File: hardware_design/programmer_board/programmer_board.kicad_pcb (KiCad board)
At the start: 2 copper layers, 27 parts, among them J1 SM06B-SRSS-TB(LF)(SN), J2 USB4800-03-A_REVA, Q1 SS8050-G, Q2 SS8050-G, U1 AP2112K-3.3TRG1, U2 TPD2S017DBVR, U3 CH340G, Y1 ECS-120-20-3X-EN-TR

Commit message: Almost routed programmer board
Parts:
- moved D1 46.7 mm to (99.3, 86.4)
- moved R3 38.2 mm to (99.3, 88.1)
- moved Q2 30.1 mm to (117.9, 95.8)
- moved R2 25.6 mm to (114.8, 92.2)
- moved C4 24.9 mm to (110.5, 90.4), turned to 180 degrees
- moved C3 24.5 mm to (110.5, 88.4), turned to 180 degrees
- moved Q1 24.1 mm to (117.9, 100.2)
- moved R1 22.3 mm to (121.4, 92.2)
- moved J1 17.1 mm to (125.3, 89.7)
- moved R4 16.3 mm to (118.1, 92.2), turned to 180 degrees
- moved C8 12.9 mm to (121.0, 96.5), turned to 90 degrees
- moved S1 12.1 mm to (125.0, 96.5), turned to 180 degrees
- moved S2 11.9 mm to (125.0, 100.1), turned to 180 degrees
- moved C9 11.9 mm to (120.9, 100.1), turned to 90 degrees
- moved Y1 11.2 mm to (106.4, 89.4)
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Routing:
- net GND: track 7.85 -> 36.5 mm, vias 3 -> 9
- net RST: track 0.00 -> 22.8 mm, vias 0 -> 2
- net BOOT: track 0.00 -> 20.4 mm
- net RTS: track 0.00 -> 18.5 mm
- net DTR: track 0.00 -> 13.6 mm
- net /USB_N: track 11.6 -> 25.0 mm
- net Net-(U3-XO): track 0.00 -> 13.2 mm
- net VBUS: track 22.7 -> 32.8 mm, vias 0 -> 2
- net /USB_P: track 14.7 -> 24.7 mm
- net Net-(C5-Pad1): track 7.80 -> 15.6 mm
- net Net-(U3-XI): track 0.00 -> 7.14 mm
- net Net-(J2-CC2): track 0.00 -> 6.66 mm
- net Net-(J2-CC1): track 0.00 -> 6.61 mm
- net +3.3V: track 11.0 -> 15.6 mm
- net Net-(J1-Pad1): track 0.00 -> 3.03 mm
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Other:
- board text added: "BOOT"
- board text added: "RST"

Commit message: Programmer board progress
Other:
- board outline added: 47.5 x 18.5 mm
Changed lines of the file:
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@@
     (pad "S2" smd rect (at 3.8 3.875 90) (size 1.2 1.8) (layers "F.Cu" "F.Paste" "F.Mask")
       (net 13 "Net-(J1-SHIELD-PadS1)") (pinfunction "SHIELD") (pintype "passive"))
+    (model "C:/Users/perry/Documents/Footprints/SM06B-SRSS-TB_LF__SN_/SM06B-SRSS-TB_LF__SN_.step"
+      (offset (xyz 0 -2 0))
+      (scale (xyz 1 1 1))
+      (rotate (xyz -90 0 0))
+    )
   )
   (footprint "SS8050-G:TRANS_SS8050-G" (layer "F.Cu")
@@
     (pad "3" smd rect (at 1.01 0) (size 0.8 0.6) (layers "F.Cu" "F.Paste" "F.Mask")
       (net 8 "RST") (pintype "passive"))
+    (model "C:/Users/perry/Documents/Footprints/SS8050-G/SS8050-G.step"
+      (offset (xyz 0 0 0))
+      (scale (xyz 1 1 1))
+      (rotate (xyz -90 0 0))
+    )
   )
   (footprint "TL6330AF200Q:SW_TL6330AF200Q" (layer "F.Cu")
@@
     (pad "4" smd rect (at 2.05 -0.8 180) (size 0.9 1) (layers "F.Cu" "F.Paste" "F.Mask")
       (net 8 "RST") (pintype "passive"))
+    (model "C:/Users/perry/Documents/Footprints/TL6330AF200Q/TL6330AF200Q.step"
+      (offset (xyz 0 0 0))
+      (scale (xyz 1 1 1))
+      (rotate (xyz -90 0 0))
+    )
   )
   (footprint "Resistor_SMD:R_0603_1608Metric" (layer "F.Cu")
@@
     (pad "16" smd roundrect (at 2.75 -4.445 270) (size 1.31 0.62) (layers "F.Cu" "F.Paste" "F.Mask") (roundrect_rratio 0.08)
       (net 1 "+3.3V") (pinfunction "VCC") (pintype "power_in"))
+    (model "C:/Users/perry/Documents/Footprints/CH340G/CH340G.step"
+      (offset (xyz 0 0 0))
+      (scale (xyz 1 1 1))
+      (rotate (xyz -90 0 0))
+    )
   )
   (footprint "Capacitor_SMD:C_0603_1608Metric" (layer "F.Cu")
@@
     (pad "5" smd roundrect (at 1.185 -0.95 270) (size 0.6 1.35) (layers "F.Cu" "F.Paste" "F.Mask") (roundrect_rratio 0.1)
       (net 1 "+3.3V") (pinfunction "VOUT") (pintype "power_in"))
+    (model "C:/Users/perry/Documents/Footprints/AP2112K-3.3TRG1/AP2112K-3.3TRG1.step"
+      (offset (xyz 0 0 0))
+      (scale (xyz 1 1 1))
+      (rotate (xyz -90 0 -90))
+    )
   )
   (footprint "TPD2S017DBVR:SOT95P280X145-6N" (layer "F.Cu")
@@
     (pad "6" smd roundrect (at 1.255 -0.95) (size 1.21 0.58) (layers "F.Cu" "F.Paste" "F.Mask") (roundrect_rratio 0.07)
       (net 28 "/USB_P") (pinfunction "CH2_OUT") (pintype "output"))
+    (model "C:/Users/perry/Documents/Footprints/TPD2S017DBVR/TPD2S017DBVR.step"
+      (offset (xyz 0 0 0))
+      (scale (xyz 1 1 1))
+      (rotate (xyz -90 0 0))
+    )
   )
   (footprint "Resistor_SMD:R_0603_1608Metric" (layer "F.Cu")
@@
     (pad "4" smd rect (at 2.05 -0.8 180) (size 0.9 1) (layers "F.Cu" "F.Paste" "F.Mask")
       (net 7 "BOOT") (pintype "passive"))
+    (model "C:/Users/perry/Documents/Footprints/TL6330AF200Q/TL6330AF200Q.step"
+      (offset (xyz 0 0 0))
+      (scale (xyz 1 1 1))
+      (rotate (xyz -90 0 0))
+    )
   )
   (footprint "Resistor_SMD:R_0603_1608Metric" (layer "F.Cu")
@@
     (pad "3" smd rect (at 1.01 0) (size 0.8 0.6) (layers "F.Cu" "F.Paste" "F.Mask")
       (net 7 "BOOT") (pintype "passive"))
+    (model "C:/Users/perry/Documents/Footprints/SS8050-G/SS8050-G.step"
+      (offset (xyz 0 0 0))
+      (scale (xyz 1 1 1))
+      (rotate (xyz -90 0 0))
+    )
   )
   (footprint "Resistor_SMD:R_0603_1608Metric" (layer "F.Cu")
@@
     (property "Sheetname" "")
     (attr smd)
-    (fp_text reference "J2" (at 3.0635 -7.112 -180) (layer "F.SilkS") hide
-        (effects (font (size 1 1) (thickness 0.15)))
-    )
-    (fp_text value "USB4800-03-A_REVA" (at 7.975 -7.635 -90) (layer "F.Fab")
-        (effects (font (size 1 1) (thickness 0.15)))
-    )
-    (fp_text user "PCB EDGE" (at 5.5 1.9 -90) (layer "F.Fab")
+    (fp_text reference "J2" (at 3.0635 -7.112) (layer "F.SilkS") hide
+        (effects (font (size 1 1) (thickness 0.15)))
+    )
+    (fp_text value "USB4800-03-A_REVA" (at 7.975 -7.635 90) (layer "F.Fab")
+        (effects (font (size 1 1) (thickness 0.15)))
+    )
+    (fp_text user "PCB EDGE" (at 5.5 1.9 90) (layer "F.Fab")
         (effects (font (size 0.64 0.64) (thickness 0.15)))
     )
@@
     (pad "S4" thru_hole oval (at 4.61 -4.5 270) (size 1 2) (drill oval 0.6 1.6) (layers "*.Cu" "*.Mask")
       (net 14 "Net-(J2-SHIELD-PadS1)") (pinfunction "SHIELD") (pintype "passive"))
+    (model "C:/Users/perry/Documents/Footprints/USB4800-03-A_REVA/USB4800-03-A_REVA.step"
+      (offset (xyz 0 0 0))
+      (scale (xyz 1 1 1))
+      (rotate (xyz -90 0 0))
+    )
   )
   (footprint "Inductor_SMD:L_0805_2012Metric" (layer "F.Cu")
@@
     (pad "2" smd rect (at 2.75 0 270) (size 3.5 1.2) (layers "F.Cu" "F.Paste" "F.Mask")
       (net 5 "Net-(U3-XI)") (pintype "passive"))
-  )
+    (model "C:/Users/perry/Documents/Footprints/ECS-122.8-20-3X-EN-TR/ECS-122.8-20-3X-EN-TR.step"
+      (offset (xyz 0 0 0))
+      (scale (xyz 1 1 1))
+      (rotate (xyz -90 0 0))
+    )
+  )
+  (gr_line (start 83.448026 85.852) (end 83.439 101.854)
+    (stroke (width 0.1) (type default)) (layer "Edge.Cuts"))
+  (gr_line (start 130.927974 101.854) (end 130.927974 85.852)
+    (stroke (width 0.1) (type default)) (layer "Edge.Cuts"))
+  (gr_arc (start 130.927974 101.854) (mid 130.556 102.752026) (end 129.657974 103.124)
+    (stroke (width 0.1) (type default)) (layer "Edge.Cuts"))
+  (gr_arc (start 83.448026 85.852) (mid 83.82 84.953974) (end 84.718026 84.582)
+    (stroke (width 0.1) (type default)) (layer "Edge.Cuts"))
+  (gr_arc (start 84.709 103.124) (mid 83.810974 102.752026) (end 83.439 101.854)
+    (stroke (width 0.1) (type default)) (layer "Edge.Cuts"))
+  (gr_arc (start 129.657974 84.582) (mid 130.556 84.953974) (end 130.927974 85.852)
+    (stroke (width 0.1) (type default)) (layer "Edge.Cuts"))
+  (gr_line (start 84.709 103.124) (end 129.657974 103.124)
+    (stroke (width 0.1) (type default)) (layer "Edge.Cuts"))
+  (gr_line (start 84.718026 84.582) (end 129.657974 84.582)
+    (stroke (width 0.1) (type default)) (layer "Edge.Cuts"))
   (gr_text "RST" (at 130.0755 101.816 90) (layer "F.SilkS")
     (effects (font (size 1 1) (thickness 0.25) bold) (justify left bottom))

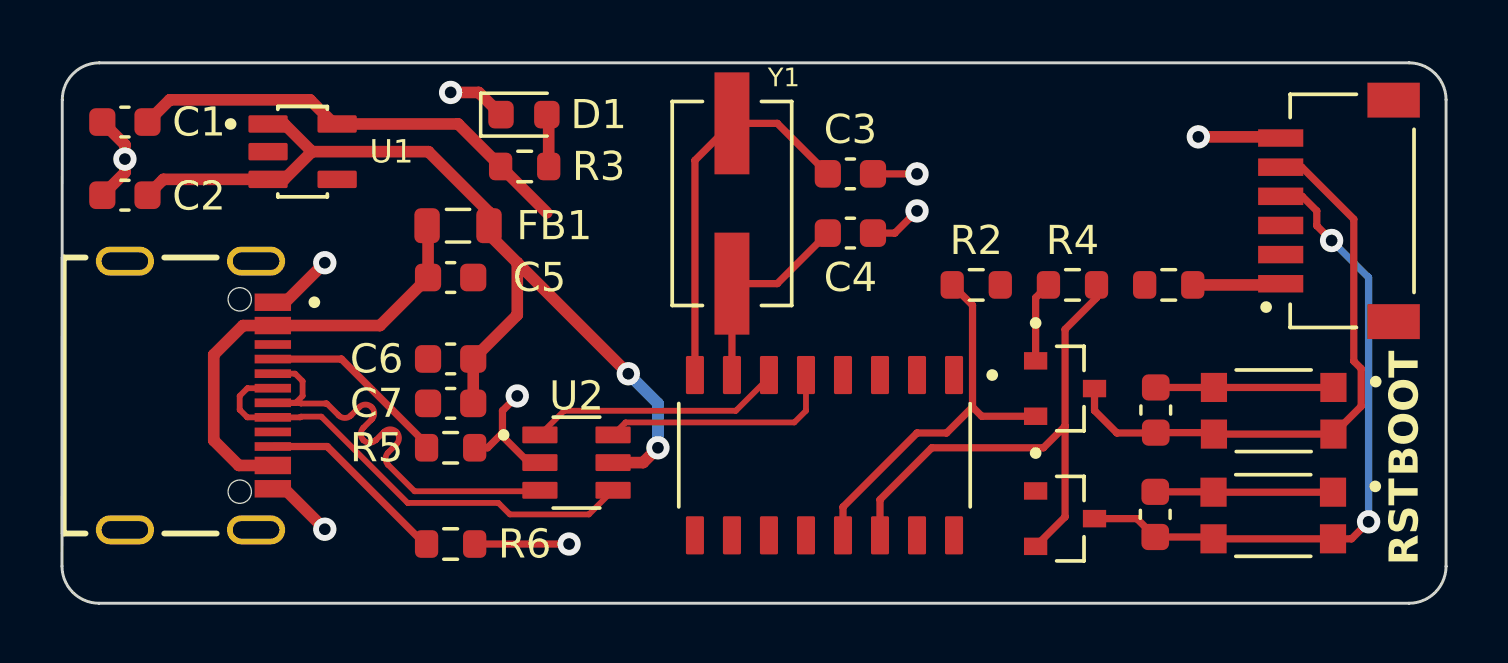
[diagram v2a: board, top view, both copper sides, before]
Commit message: Programmer board PCB
Programmer board PCB finished.
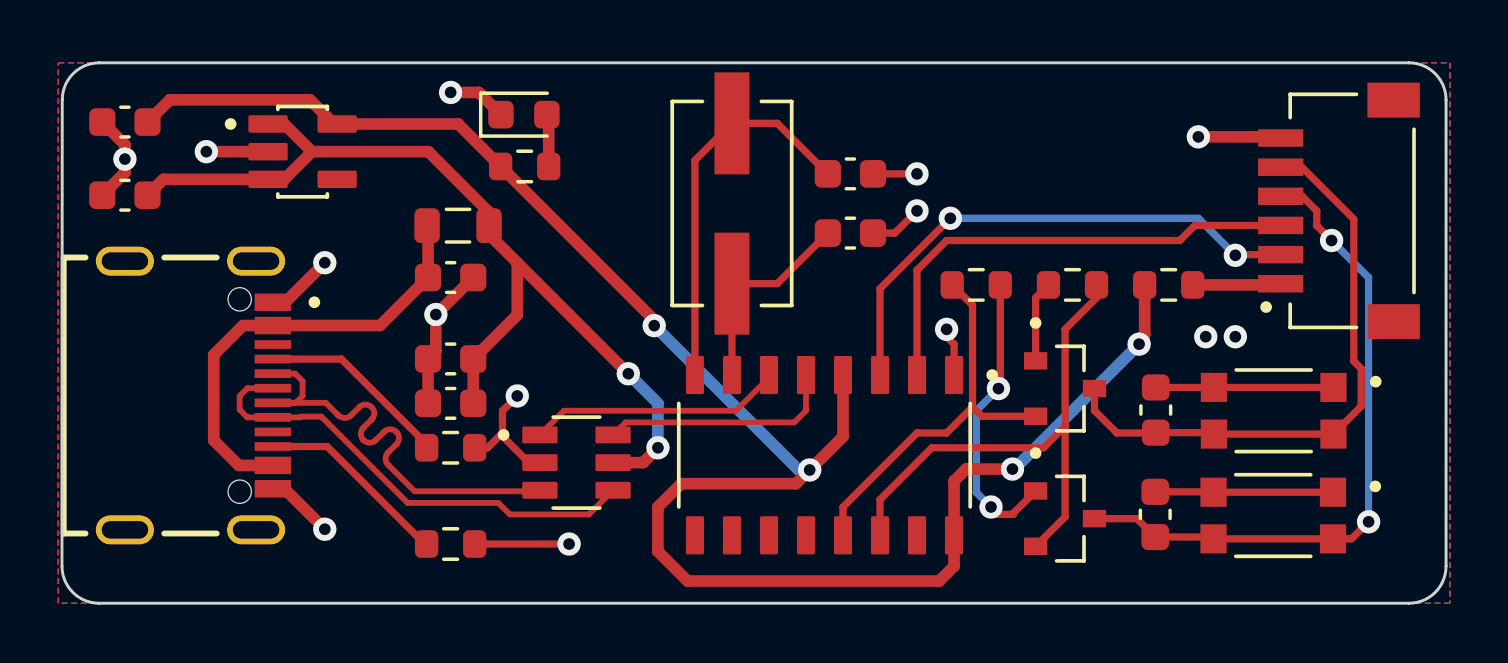
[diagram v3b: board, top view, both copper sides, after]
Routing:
- net +3.3V: track 15.6 -> 63.9 mm, vias 0 -> 4
- net RX: track 0.13 -> 18.5 mm, vias 0 -> 2
- net TX: track 0.46 -> 17.2 mm
- net Net-(Q1-Pad1): track 0.00 -> 10.5 mm, vias 0 -> 2
- net GND: track 36.5 -> 45.4 mm, vias 9 -> 14
- added copper zone on B.Cu, net GND
- added copper zone on F.Cu, net GND
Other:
- board text added: "ESP32 flasher."
- board text added: "GND BOOT RST TX RX 3V3 OUT"
- board text added: "Perry Petiet"
